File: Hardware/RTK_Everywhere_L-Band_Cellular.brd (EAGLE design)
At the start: 165.5 x 131.1 mm, 409 parts, among them J3 MICRO-SD-PUSH-PUSH-EXT-PIN, J4 Vertical Qwiic Connector, J9 MAGJACK-POE, U1 ESP32-WROVER-IE, U10 POE_PSU-DP990X, U11 MCP6021T, U12 AP7361C-33, U13 MCP6021T, U14 BP2G1+_POWER_SPLITTER, U15 USB251XB_USB2514B, U16 SN74AVC4T774PW, U17 URB2405YMD, U2 CH340C, U3 XC6222B331MR-G, U4 U-BLOX_ZED-F9P, U5 U-BLOX_NEO-D9S-00B, U6 XC6222B331MR-G, U7 W5500, U8 LARA-R6001D, U9 74LVC4066D_QUAD_BILATERAL_SWI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, Y1 25MHz, Y2 24MHz

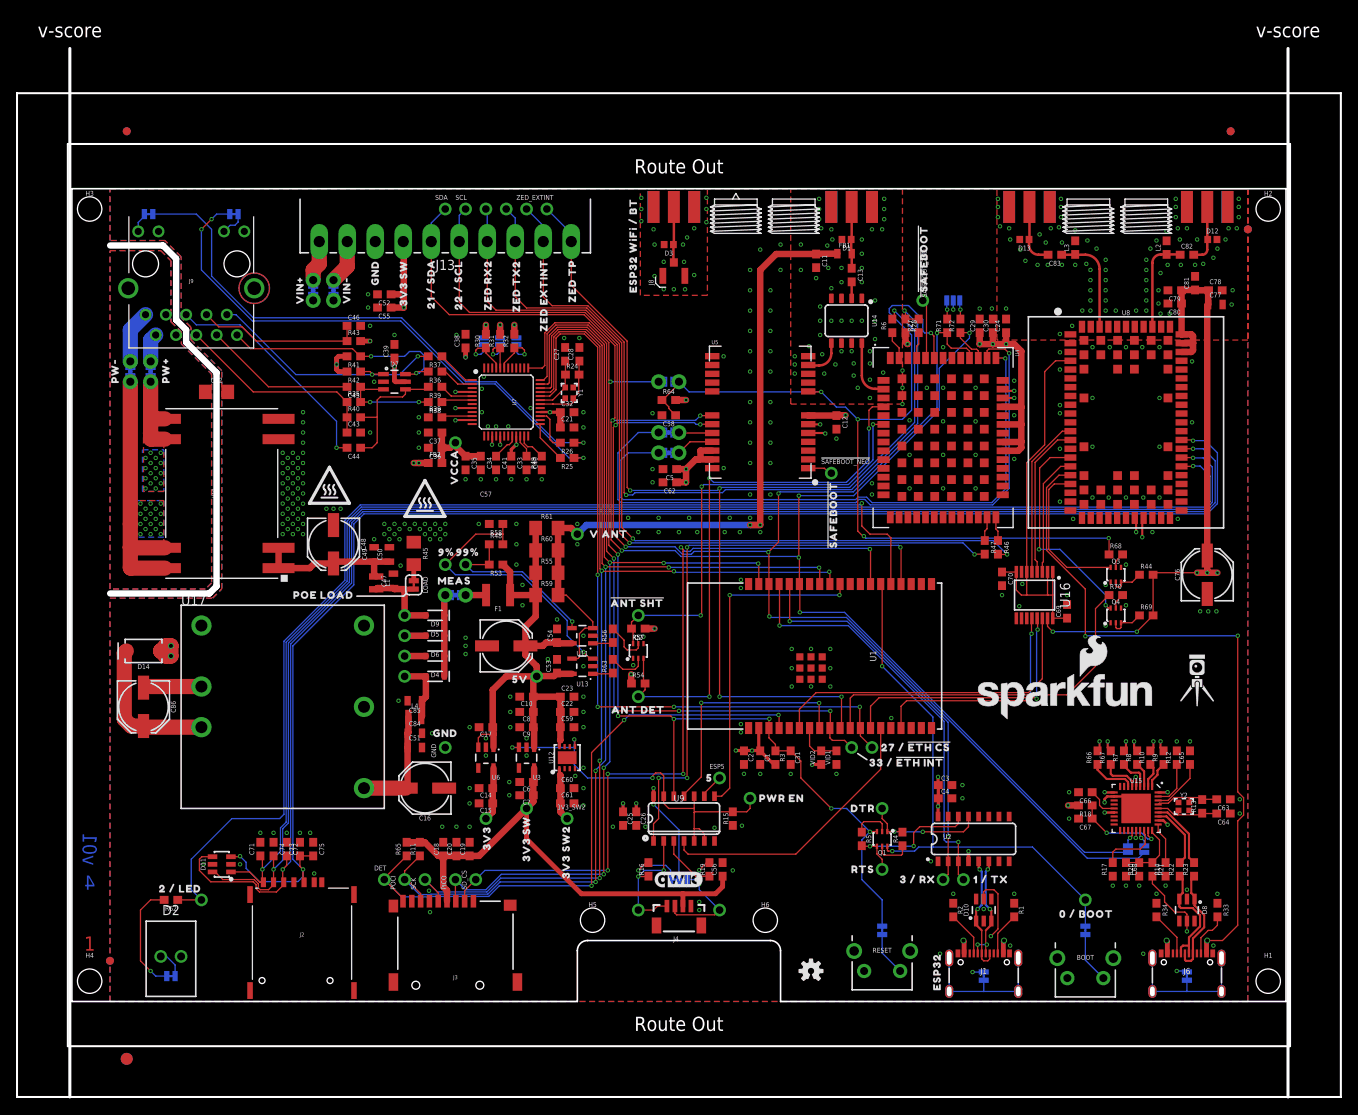
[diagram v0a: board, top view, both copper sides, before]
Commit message: Add no L-Band bypass. Update silk. Increase display cutout.
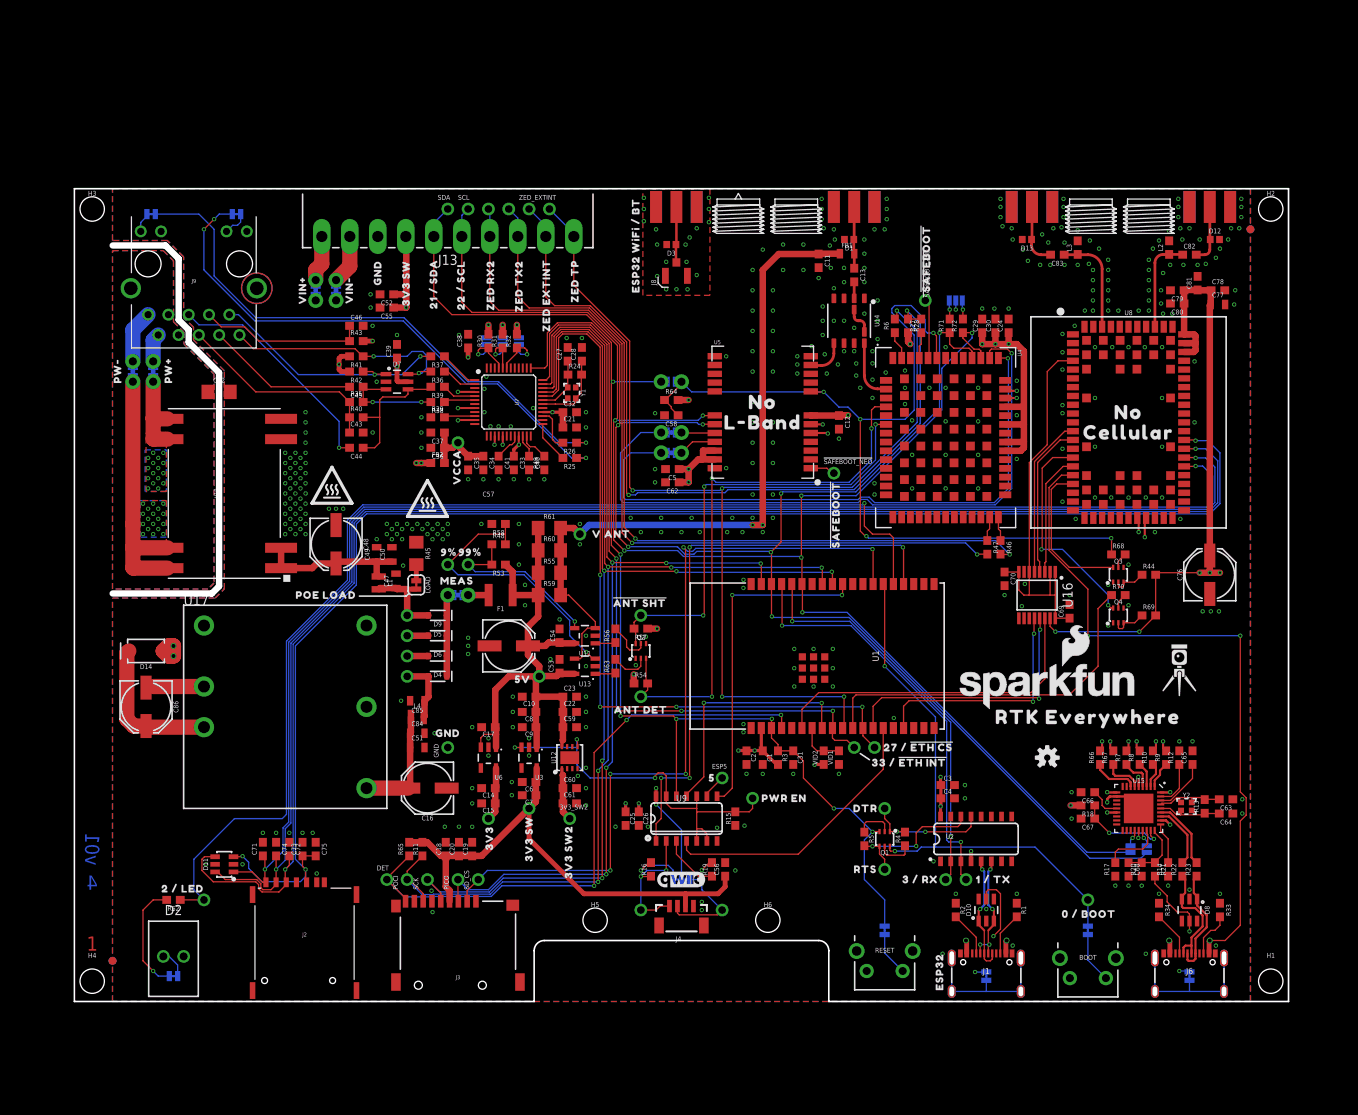
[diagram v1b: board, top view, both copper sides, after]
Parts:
- removed E$1, E$2, E$3, E$4: (no value), SparkFun-Aesthetics:FIDUCIAL-1X2
- removed E$5, E$6: (no value), SparkFun-Retired:FIDUCIAL-1.5X3
- added FRAME1: FRAME-LEDGER, SparkFun-Aesthetics:CREATIVE_COMMONS
- added FRAME2: FRAME-LEDGERNO_FOOTPRINT, SparkFun-Aesthetics:DUMMY
- added JPP1, JPP2: NO PASTE, SparkFun-Jumpers:SMT-JUMPER_2_SOIC-PAD_NO-PASTE
- added LOGO1: SPECIAL_INSTRUCTIONS-ORDERING, SparkFun-Aesthetics:ORDERING_INSTRUCTIONS
- added U$2, U$90: (no value), output:RTK_EVERYWHERE0
- added U$91, U$92: (no value), output:NO0
- added U$96: (no value), output:CELLULAR2
- added U$97: (no value), output:L#BAND1
- moved LOGO4 39.8 mm to (121.9, 30.5)
- moved LOGO6 2.56 mm to (125.5, 44.5)
- moved U$152 2.56 mm to (138.4, 41.4)
- moved LOGO5 2.56 mm to (121.9, 39.4)
- moved J13 0.71 mm to (47.0, 98.4)
- moved C68 0.32 mm to (132.1, 16.5)
- moved H1 0.32 mm to (149.9, 2.54)
- moved H2 0.32 mm to (149.9, 99.1)
- moved JP2 0.32 mm to (134.4, 19.1)
- moved R67 0.32 mm to (130.2, 30.5)
- moved U8 0.32 mm to (132.1, 72.4)
- moved !SAFEBOOT_ZED! 0.32 mm to (106.7, 87.6)
- moved ANT_DET 0.32 mm to (71.1, 38.1)
- moved ANT_SHT 0.32 mm to (71.1, 48.3)
- moved C12 0.32 mm to (95.9, 72.4)
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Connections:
- net N$42 renamed ANT
- new net BYPASS: JPP1.1, JPP2.1
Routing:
- net BYPASS: track 0.00 -> 3.47 mm
- net 3.3V_SW: track 146.4 -> 147.1 mm
- net VIN-: track 6.29 -> 6.93 mm
- net VIN+: track 5.90 -> 6.53 mm
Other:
- board size 165.5 x 131.1 mm -> 151.8 x 101.6 mm
- board text added: "Controlled Impedance: JLC7628 Material: TG155 4-Layers Thickness: 1.6mm Outer Copper: 1oz Inner Copper: 0.5oz Finish: HASL Lead Free Red Solder Resist White Silkscreen"
- board text added: "Dimensions In Inches"
- board text added: "Paul Clark"
- board text added: "V-Score To V-Score"
- board text removed: "Route Out"
- board text removed: "v-score"

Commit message: Update RF Bypass SOIC Pad jumpers
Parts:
- removed JPP1, JPP2: NO PASTE, SparkFun-Jumpers:SMT-JUMPER_2_SOIC-PAD_NO-PASTE
- added BYPASS1, BYPASS2: NO PASTE, SparkFun-Jumpers:SMT-JUMPER_2_SOIC-PAD_NO-PASTE
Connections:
- net BYPASS: now also BYPASS1.1, BYPASS2.1; no longer JPP1.1, JPP2.1
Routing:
- net BYPASS: track 3.47 -> 4.03 mm
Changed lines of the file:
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@@
 <drawing>
 <settings>
-<setting alwaysvectorfont="yes"/>
+<setting alwaysvectorfont="no"/>
 <setting verticaltext="up"/>
 </settings>
@@
 <element name="U$79" library="output" package="UART14" value="" x="74.93" y="72.898" smashed="yes" rot="MR0"/>
 <element name="U$89" library="output" package="4_#_#SD_CS#15" value="" x="50.8" y="10.922" smashed="yes" rot="MR270"/>
-<element name="JPP1" library="SparkFun-Jumpers" package="SMT-JUMPER_2_SOIC-PAD_NO-PASTE" value="NO PASTE" x="97.79" y="86.487" smashed="yes" rot="R90"/>
-<element name="JPP2" library="SparkFun-Jumpers" package="SMT-JUMPER_2_SOIC-PAD_NO-PASTE" value="NO PASTE" x="99.06" y="83.693" smashed="yes" rot="R270"/>
+<element name="BYPASS1" library="SparkFun-Jumpers" package="SMT-JUMPER_2_SOIC-PAD_NO-PASTE" value="NO PASTE" x="97.79" y="85.09" smashed="yes" rot="R90">
+<attribute name="VALUE" value="NO PASTE" x="97.79" y="85.09" size="1.778" layer="27" rot="R90" display="off"/>
+</element>
+<element name="BYPASS2" library="SparkFun-Jumpers" package="SMT-JUMPER_2_SOIC-PAD_NO-PASTE" value="NO PASTE" x="99.06" y="85.09" smashed="yes" rot="R270">
+<attribute name="VALUE" value="NO PASTE" x="99.06" y="85.09" size="1.778" layer="27" rot="R270" display="off"/>
+</element>
 <element name="U$2" library="output" package="RTK_EVERYWHERE0" value="" x="127" y="35.56" smashed="yes"/>
 <element name="U$90" library="output" package="RTK_EVERYWHERE0" value="" x="119.38" y="45.72" smashed="yes" rot="MR0"/>
@@
 </signal>
 <signal name="BYPASS">
-<contactref element="JPP1" pad="1"/>
-<contactref element="JPP2" pad="1"/>
-<wire x1="97.79" y1="86.487" x2="97.79" y2="85.598" width="0.348996875" layer="1"/>
-<wire x1="97.79" y1="85.598" x2="98.298" y2="85.09" width="0.348996875" layer="1" curve="90"/>
-<wire x1="98.298" y1="85.09" x2="98.552" y2="85.09" width="0.348996875" layer="1"/>
-<wire x1="98.552" y1="85.09" x2="99.06" y2="84.582" width="0.348996875" layer="1" curve="-90"/>
-<wire x1="99.06" y1="84.582" x2="99.06" y2="83.693" width="0.348996875" layer="1"/>
+<contactref element="BYPASS1" pad="1"/>
+<contactref element="BYPASS2" pad="1"/>
+<wire x1="97.79" y1="86.84" x2="97.79" y2="85.725" width="0.348996875" layer="1"/>
+<wire x1="97.79" y1="85.725" x2="98.425" y2="85.09" width="0.348996875" layer="1" curve="90"/>
+<wire x1="98.425" y1="85.09" x2="99.06" y2="84.455" width="0.348996875" layer="1" curve="-90"/>
+<wire x1="99.06" y1="84.455" x2="99.06" y2="83.34" width="0.348996875" layer="1"/>
 </signal>
 </signals>

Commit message: Add V10 PCB files
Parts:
- removed Q3, Q4: (no value), SparkFun-DiscreteSemi:SC70-6
- removed R69: 10k, SparkFun-Resistors:0603
- added D15, D16, D17, D18, D19, D20: PESD0402-0402, SparkFun-DiscreteSemi:0402
- added Q5, Q6: 310mA/60V/1.6Ω, SparkFun-DiscreteSemi:SOT323
- added R50, R51, R52: 100k, SparkFun-Resistors:0603
- added RXD, TXD, VCCIO: TEST-POINTPOGO_PTH, SparkFun-Connectors:1X01_NO_SILK
- added SPWR, TPWR: JUMPER-SMT_3_1-NC_TRACE_SILK, SparkFun-Jumpers:SMT-JUMPER_3_1-NC_TRACE_SILK
- added U$103: (no value), output:13_#_TXDI15
- added U$108: (no value), output:14_#_RXDO0
- added U$110, U$112: (no value), output:LARA_ON0
- added U$115, U$116: (no value), output:VCCIO0
- added U$117: (no value), output:#3V3_SW_EN#0
- added U$118: (no value), output:#3V3_SW2_EN#0
- added U18: 74HC1G04, SparkFun-IC-Logic:SOT353
- R44: value 10k -> 100k
- U$73: device output:50 -> output:14_#_RXDO0
- U$75: device output:50 -> output:13_#_TXDI15
- moved R44 37.6 mm to (127.1, 16.5), turned to 90 degrees
- moved U$75 32.3 mm to (112.1, 29.2), flipped to the top
- moved U$73 31.9 mm to (111.6, 31.8)
- moved LOGO7 22.5 mm to (130.8, 71.1)
- moved LOGO8 22.5 mm to (127.3, 76.2)
- moved U$90 22.5 mm to (125.7, 67.3)
- moved U$153 22.5 mm to (114.3, 73.3)
- moved U$48 3.56 mm to (133.3, 17.2)
- moved U$135 3.43 mm to (47.0, 30.1)
- moved LOGO4 2.54 mm to (124.5, 30.5)
- moved LOGO5 2.54 mm to (124.5, 39.4)
- moved LOGO6 2.54 mm to (128.0, 44.5)
- moved R68 2.54 mm to (128.3, 55.9), turned to 90 degrees
- moved U$152 2.54 mm to (141.0, 41.4)
- moved U$2 2.54 mm to (129.5, 35.6)
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- renumbered ESP5 to LARA_ON, JP1 to USB251SDA, JP2 to USB251SCL
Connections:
- net ESP26/LARA_ON renamed ESP26/LARA_PWR_ON
- net ESP5 renamed ESP5/LARA_ON
- removed net N$37: LARA_ON.1, U9.9
- removed net N$57: U15.22, USB251SDA.2
- removed net N$58: U15.24, USB251SCL.2
- removed net N$59: Q4.2, Q4.3, R69.1
- removed net N$60: Q3.5, R68.2
- new net LARA_ON: LARA_ON.1, U16.11, U9.9
- new net N$22: R50.1, SPWR.3
- new net N$26: SPWR.2, U3.3
- new net N$31: R51.1, TPWR.3
- new net N$39: TPWR.2, U12.5
- new net N$42: Q6.1, R68.2
- new net USB251SCL: R52.2, U15.24, USB251SCL.2
- new net USB251SDA: R44.2, U15.22, USB251SDA.2
- net 3.3V_SW2: now also U18.5; no longer R44.2, R69.2
- net 5V: now also R50.2, R51.2
- net ESP13/LARA_TXDI: now also TXD.1
- net ESP14/LARA_RXDO: now also RXD.1
- net ESP21/SDA: now also D15.1
- net ESP22/SCL: now also D16.1
- net ESP25/TP: now also D20.1
- net GND: now also D15.2, D16.2, D17.2, D18.2, D19.2, D20.2, Q5.2, Q6.2, R44.1, R52.1, U18.3; no longer Q3.1, Q3.4, Q4.1, Q4.4
- net GNSS_!RESET!: now also U18.2; no longer R68.1
- net LARA_!RESET!: now also Q6.3; no longer Q3.6
- net LARA_PWR_ON: now also Q5.3; no longer Q4.6
- net N$16: now also R68.1, U18.4; no longer Q3.2, Q3.3, R44.1
- net N$65: now also Q5.1; no longer Q4.5
- net PWREN: now also SPWR.1, TPWR.1; no longer U12.5, U3.3
- net VCCIO: now also VCCIO.1
- net ZED_EXTINT: now also D19.1
- net ZED_RX2: now also D17.1
- net ZED_TX2: now also D18.1
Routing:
- net LARA_ON: track 0.00 -> 59.5 mm, vias 0 -> 1
- net N$31: track 0.00 -> 17.5 mm, vias 0 -> 1
- net N$22: track 0.00 -> 9.95 mm, vias 0 -> 1
- net USB251SDA: track 0.00 -> 9.37 mm, vias 0 -> 1
- net USB251SCL: track 0.00 -> 9.24 mm, vias 0 -> 1
- net ESP13/LARA_TXDI: track 29.8 -> 38.8 mm
- net ESP14/LARA_RXDO: track 34.1 -> 40.3 mm
- net LARA_!RESET!: track 19.1 -> 14.1 mm
- net VCCIO: track 52.0 -> 57.0 mm
- net N$59: track 4.65 -> 0.00 mm
- net ESP0/!BOOT!: track 67.1 -> 70.7 mm
- net RD-: track 28.9 -> 32.1 mm
- net N$37: track 3.07 -> 0.00 mm
- net N$26: track 0.00 -> 3.03 mm, vias 0 -> 1
- net N$39: track 0.00 -> 2.84 mm, vias 0 -> 1
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- added copper zone on layer 15, net 3.3_SW
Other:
- board text added: "v10"
- board text removed: "v01"
